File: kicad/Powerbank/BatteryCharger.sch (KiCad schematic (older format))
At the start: 1 part

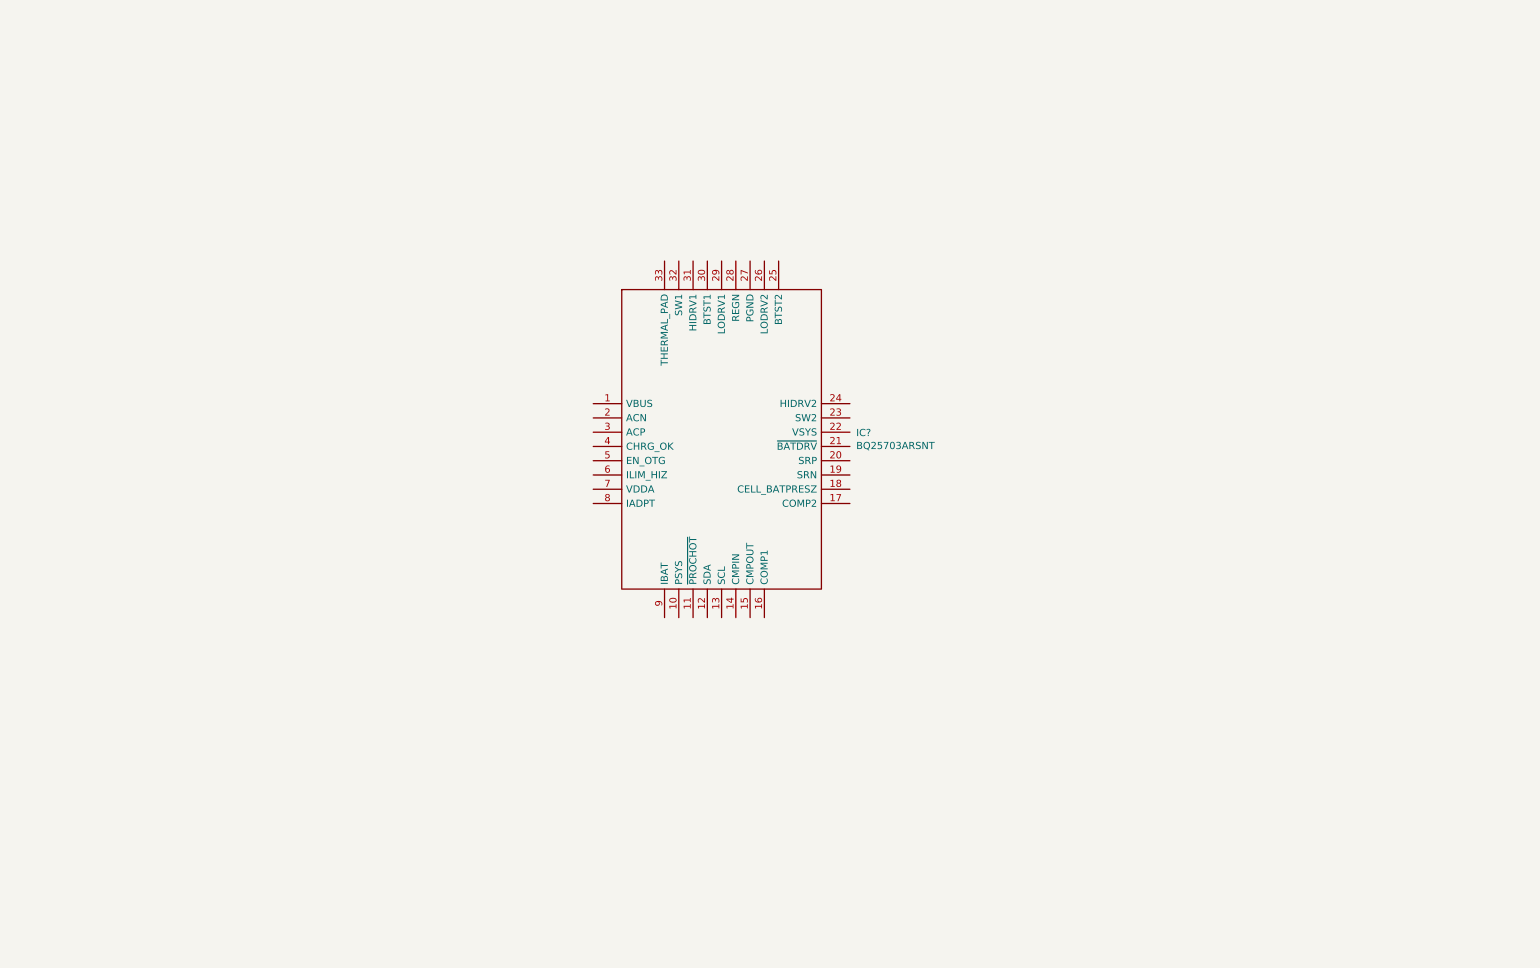
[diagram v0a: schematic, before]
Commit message: Battery charger completed according to reference guide
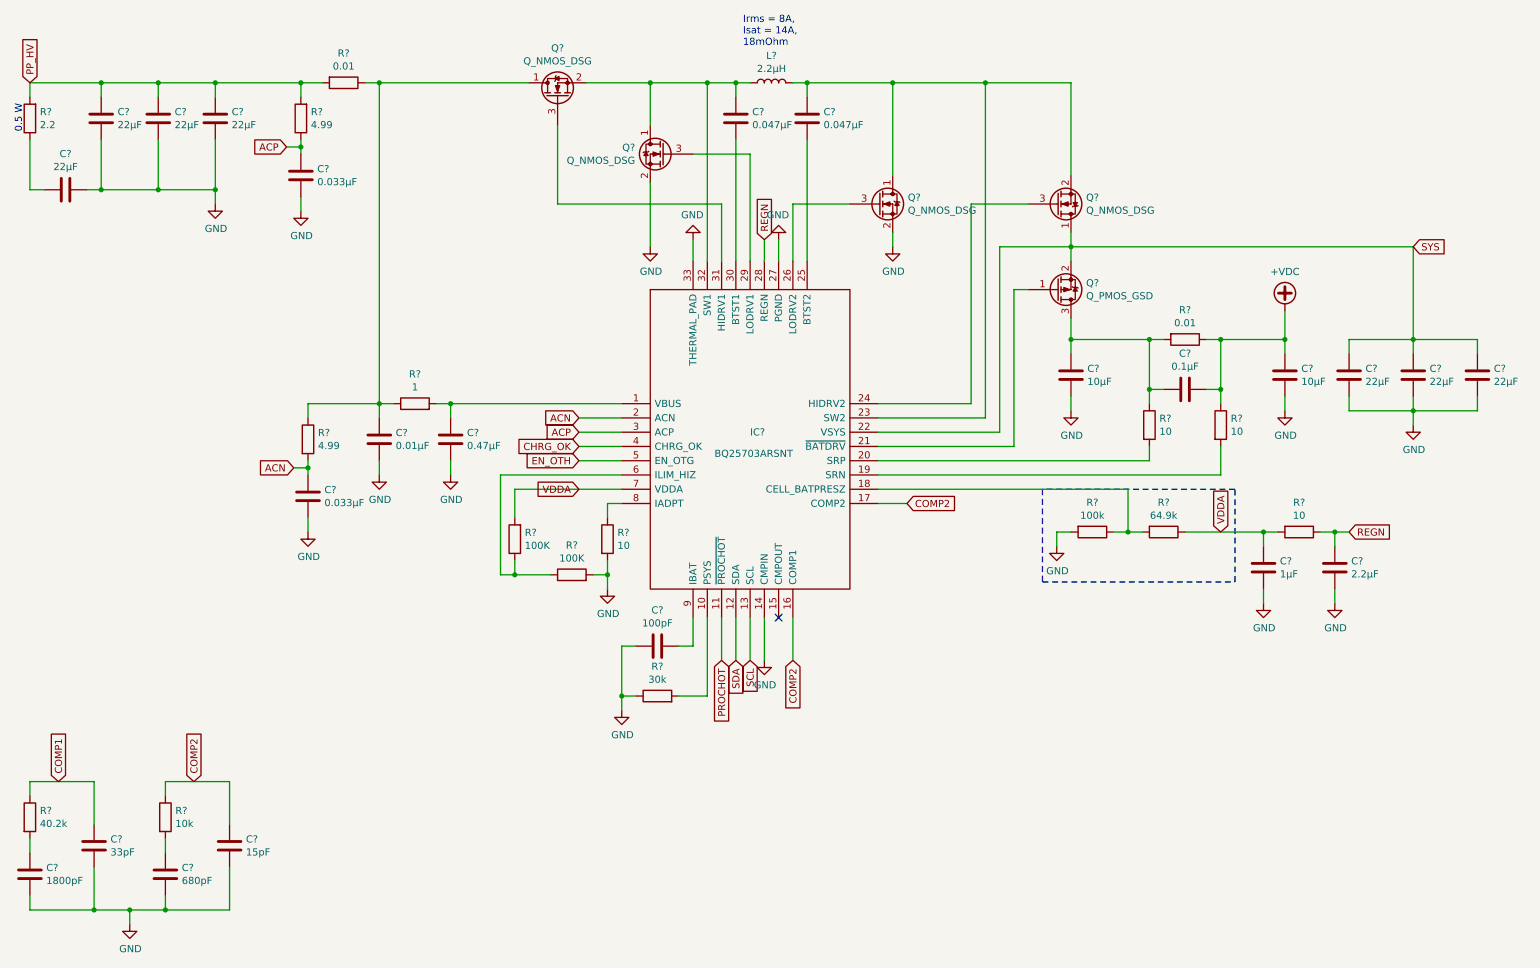
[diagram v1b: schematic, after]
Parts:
- added C?: 1800pF, symbol Device:C
- added C?: 680pF, symbol Device:C
- added C?: 15pF, symbol Device:C
- added C?: 33pF, symbol Device:C
- added C?: 0.1µF, symbol Device:C
- added C? (x2): 10µF, symbol Device:C
- added C? (x7): 22µF, symbol Device:C
- added C? (x2): 0.047µF, symbol Device:C
- added C?: 100pF, symbol Device:C
- added C?: 0.01µF, symbol Device:C
- added C?: 0.47µF, symbol Device:C
- added C? (x2): 0.033µF, symbol Device:C
- added C?: 1µF, symbol Device:C
- added C?: 2.2µF, symbol Device:C
- added L?: 2.2µH, symbol Device:L
- added Q?: Q_PMOS_GSD, symbol Device:Q_PMOS_GSD
- added Q? (x4): Q_NMOS_DSG, symbol Device:Q_NMOS_DSG
- added R?: 40.2k, symbol Device:R
- added R?: 10k, symbol Device:R
- added R? (x4): 10, symbol Device:R
- added R? (x2): 0.01, symbol Device:R
- added R?: 100k, symbol Device:R
- added R?: 64.9k, symbol Device:R
- added R? (x2): 100K, symbol Device:R
- added R?: 30k, symbol Device:R
- added R?: 1, symbol Device:R
- added R? (x2): 4.99, symbol Device:R
- added R?: 2.2, symbol Device:R
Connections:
- net at IC?.1 (VBUS): now also C?.1, R?.2
- net at IC?.10 (PSYS): now also R?.2
- net PROCHOT: now reaches IC?.11 (~PROCHOT)
- net SDA: now reaches IC?.12 (SDA)
- net SCL: now reaches IC?.13 (SCL)
- net GND: now reaches IC?.14 (CMPIN)
- net GND: now also IC?.27 (PGND), IC?.33 (THERMAL_PAD), C?.1, C?.1, C?.1, C?.1, C?.1, C?.1, C?.1, C?.1, C?.1, C?.1, C?.1, C?.2, C?.2, C?.2, C?.2, C?.2, C?.2, C?.2, C?.2, C?.2, Q?.2 (S), Q?.2 (S), R?.1, R?.2, R?.2, R?.2
- net COMP2: now reaches IC?.16 (COMP1)
- net COMP2: now also IC?.17 (COMP2), C?.1, R?.1
- net at IC?.18 (CELL_BATPRESZ): now also R?.1, R?.2
- net at IC?.19 (SRN): now also R?.2
- net ACN: now reaches IC?.2 (ACN)
- net ACN: now also C?.1, R?.2
- net at IC?.20 (SRP): now also R?.2
- net at IC?.21 (~BATDRV): now also Q?.1 (G)
- net SYS: now reaches IC?.22 (VSYS)
- net SYS: now also C?.2, C?.2, C?.2, Q?.1 (D), Q?.2 (S)
- net at IC?.23 (SW2): now also C?.2, L?.2, Q?.1 (D), Q?.2 (S)
- net at IC?.24 (HIDRV2): now also Q?.3 (G)
- net at IC?.25 (BTST2): now also C?.1
- net at IC?.26 (LODRV2): now also Q?.3 (G)
- net REGN: now reaches IC?.28 (REGN)
- net REGN: now also C?.2, R?.1
- net at IC?.29 (LODRV1): now also Q?.3 (G)
- net ACP: now reaches IC?.3 (ACP)
- net ACP: now also C?.1, R?.1
- net at IC?.30 (BTST1): now also C?.1
- net at IC?.31 (HIDRV1): now also Q?.3 (G)
- net at IC?.32 (SW1): now also C?.2, L?.1, Q?.1 (D), Q?.2 (S)
- net CHRG_OK: now reaches IC?.4 (CHRG_OK)
- net EN_OTH: now reaches IC?.5 (EN_OTG)
- net at IC?.6 (ILIM_HIZ): now also R?.1, R?.1
- net VDDA: now reaches IC?.7 (VDDA)
- net VDDA: now also C?.2, R?.1, R?.2, R?.2
- net at IC?.8 (IADPT): now also R?.1
- net at IC?.9 (IBAT): now also C?.2
- new net: C?.1, R?.2 (x2)
- new net: C?.2, C?.2, Q?.3 (D), R?.1, R?.2
- new net: C?.1, Q?.1 (D), R?.1, R?.1, R?.1
- new net: C?.1, R?.1
- new net +VDC: C?.1, C?.2, R?.1, R?.1
- new net COMP1: C?.1, R?.1
- new net PP_HV: C?.2, C?.2, C?.2, R?.2, R?.2, R?.2
- no-connect marks 0 -> 1
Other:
- note added: "0.5 W"
- note added: "Irms = 8A, \nIsat = 14A, \n18mOhm"
- moved on the sheet: IC?

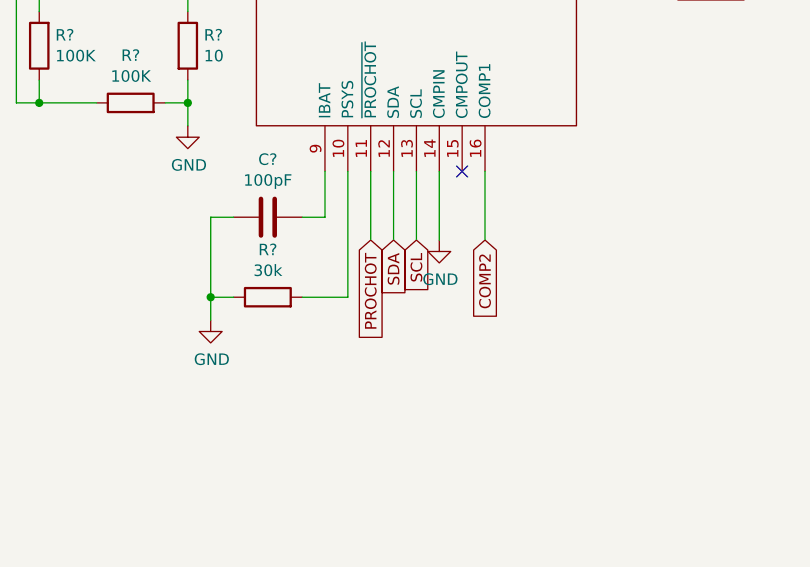
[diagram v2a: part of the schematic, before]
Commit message: Moved LDO to Buck sheet and started check of components
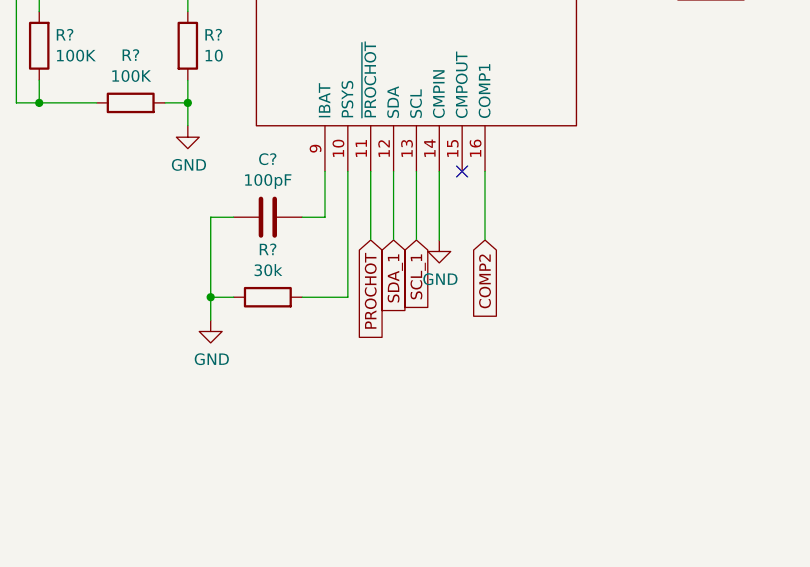
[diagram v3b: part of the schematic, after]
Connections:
- net SCL renamed SCL_1
- net SDA renamed SDA_1
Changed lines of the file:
@@
 $Descr A4 11693 8268
 encoding utf-8
-Sheet 3 8
+Sheet 3 7
 Title ""
 Date ""
@@
 	6600 4550 6800 4550
 Text GLabel 5600 5650 3    50   Input ~ 0
-SDA
+SDA_1
 Text GLabel 5700 5650 3    50   Input ~ 0
-SCL
+SCL_1
 Wire Wire Line
 	5700 5350 5700 5650

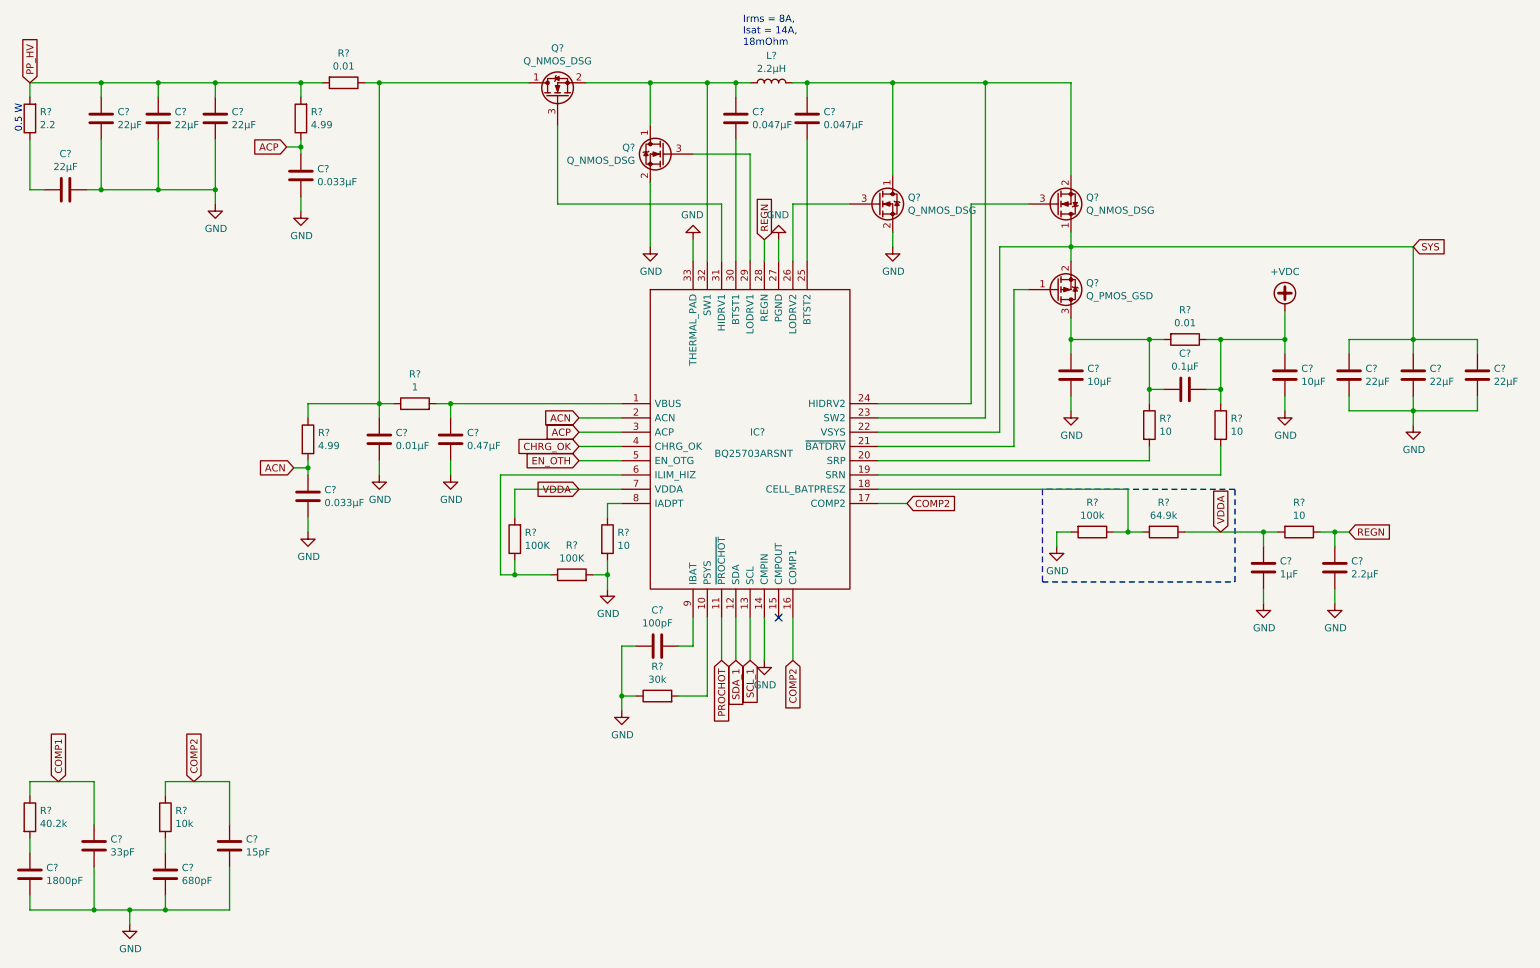
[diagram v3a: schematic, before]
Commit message: Double checked schematic towards reference design
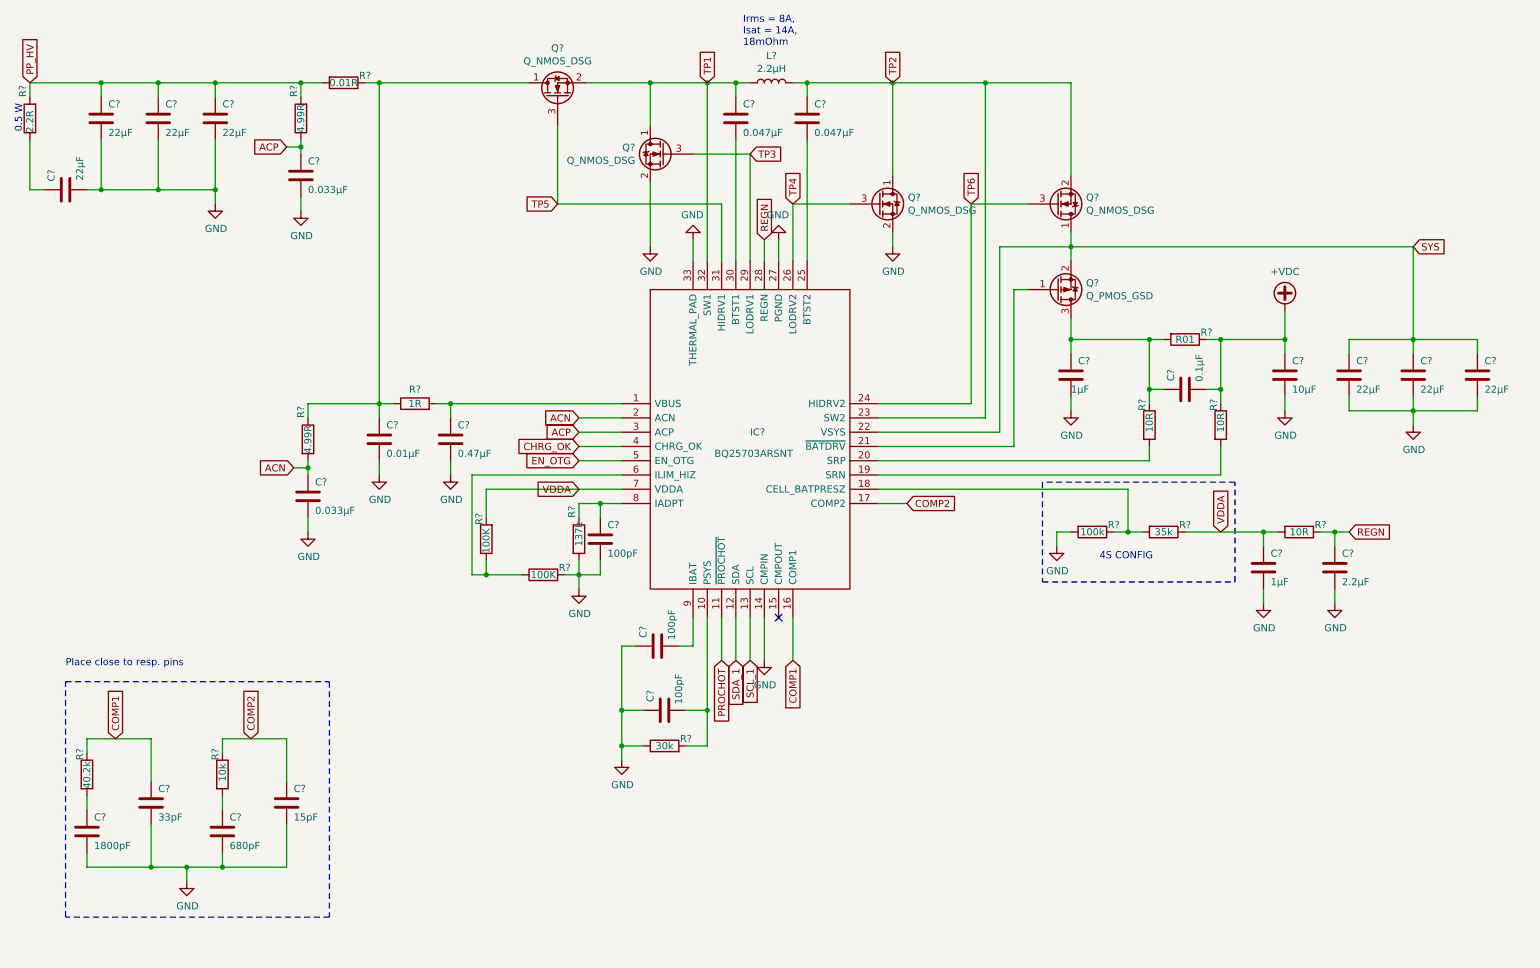
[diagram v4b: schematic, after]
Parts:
- added C? (x2): 100pF, symbol Device:C
- C?: value 10µF -> 1µF
- R? (x3): value 10 -> 10R
- R?: value 0.01 -> R01
- R?: value 10 -> 137k
- R?: value 64.9k -> 35k
- R?: value 1 -> 1R
- R? (x2): value 4.99 -> 4.99R
- R?: value 0.01 -> 0.01R
- R?: value 2.2 -> 2.2R
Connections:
- net COMP1: now also IC?.16 (COMP1)
- net COMP2: no longer IC?.16 (COMP1)
- net GND: now also C?.1, C?.2
- net at IC?.10 (PSYS), R?.2: now also C?.2
- net TP2: now reaches C?.2, IC?.23 (SW2), L?.2, Q?.1 (D), Q?.2 (S)
- net TP6: now reaches IC?.24 (HIDRV2), Q?.3 (G)
- net TP4: now reaches IC?.26 (LODRV2), Q?.3 (G)
- net TP3: now reaches IC?.29 (LODRV1), Q?.3 (G)
- net TP5: now reaches IC?.31 (HIDRV1), Q?.3 (G)
- net TP1: now reaches C?.2, IC?.32 (SW1), L?.1, Q?.1 (D), Q?.2 (S)
- net at IC?.8 (IADPT), R?.1: now also C?.1
- net EN_OTH renamed EN_OTG
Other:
- note added: "4S CONFIG"
- note added: "Place close to resp. pins"
- moved on the sheet: C?, R?

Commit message: Updated for PCB
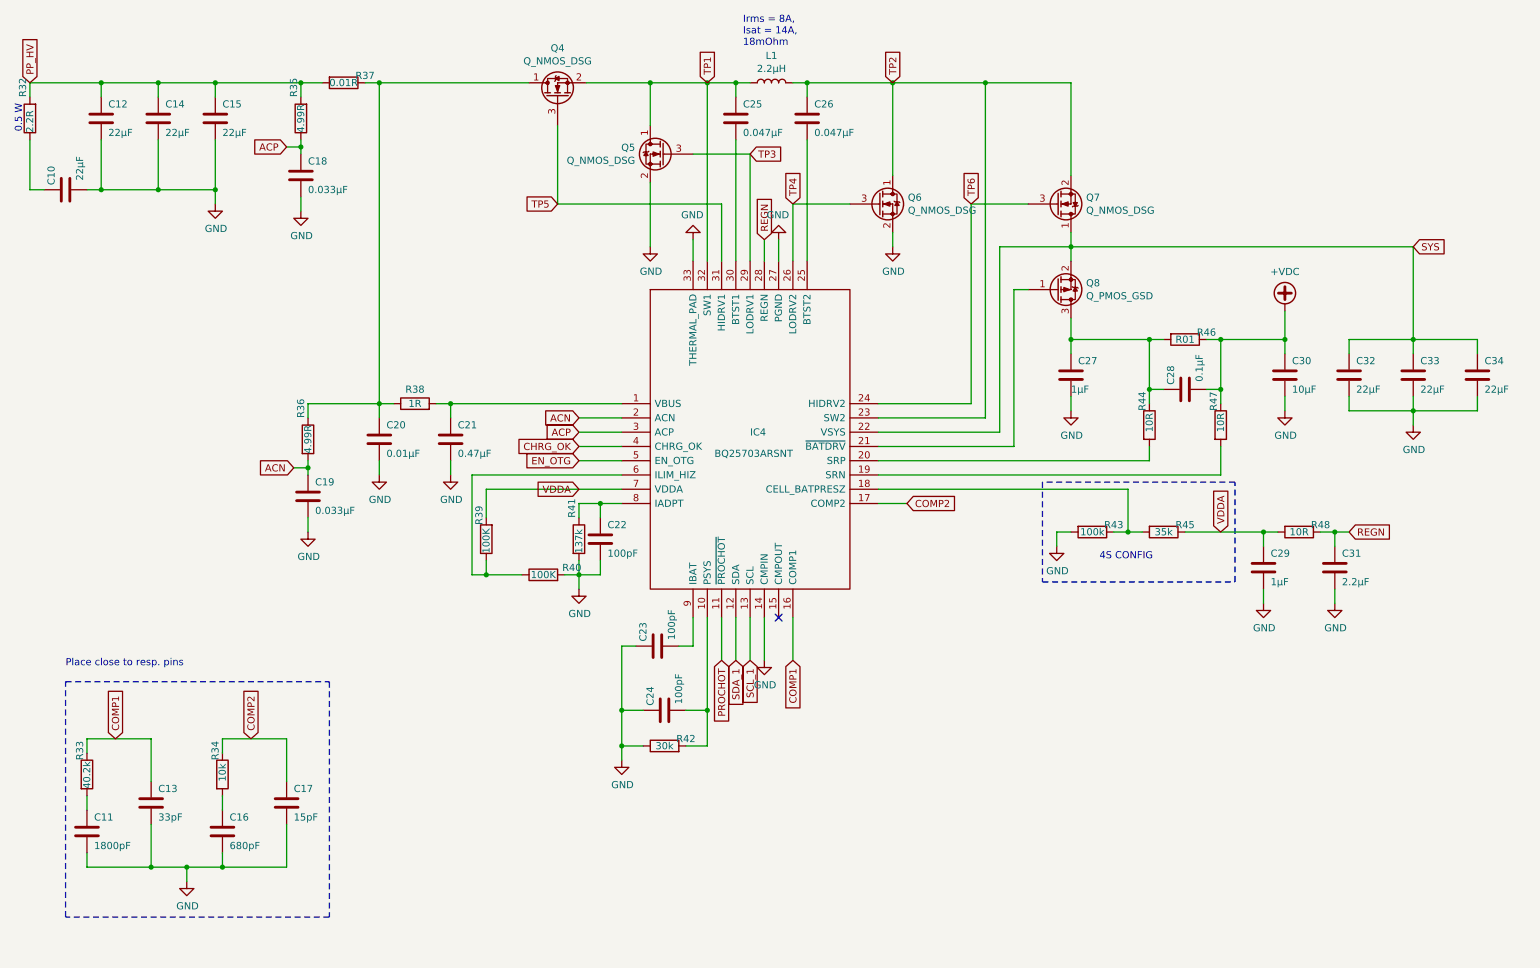
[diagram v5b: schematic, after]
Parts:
- C10, C14, C15, C32, C33, C34: renamed from C?; footprint (none) -> Capacitor_SMD:C_0805_2012Metric
- C11, C12, C13, C16, C17, C18, C19, C20, C21, C22, C23, C24, C25, C26, C27, C28, C29, C30, C31: renamed from C?; footprint (none) -> Capacitor_SMD:C_0603_1608Metric
- IC4: renamed from IC?; footprint QFN40P400X400X80-33N-D -> Powerbank:QFN40P400X400X80-33N-D
- L1: renamed from L?; footprint (none) -> Powerbank:WE_Inductor_7443330220
- R33, R34, R35, R36, R37, R38, R39, R40, R41, R42, R43, R44, R45, R46, R47, R48: renamed from R?; footprint (none) -> Resistor_SMD:R_0603_1608Metric
- gave numbers to parts that had none: 6
